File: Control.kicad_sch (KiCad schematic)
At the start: 65 parts, among them U2 LT6108IMS8-1-TRPBF, U3 LM139ADRG4, U5 LT6108IMS8-1-TRPBF

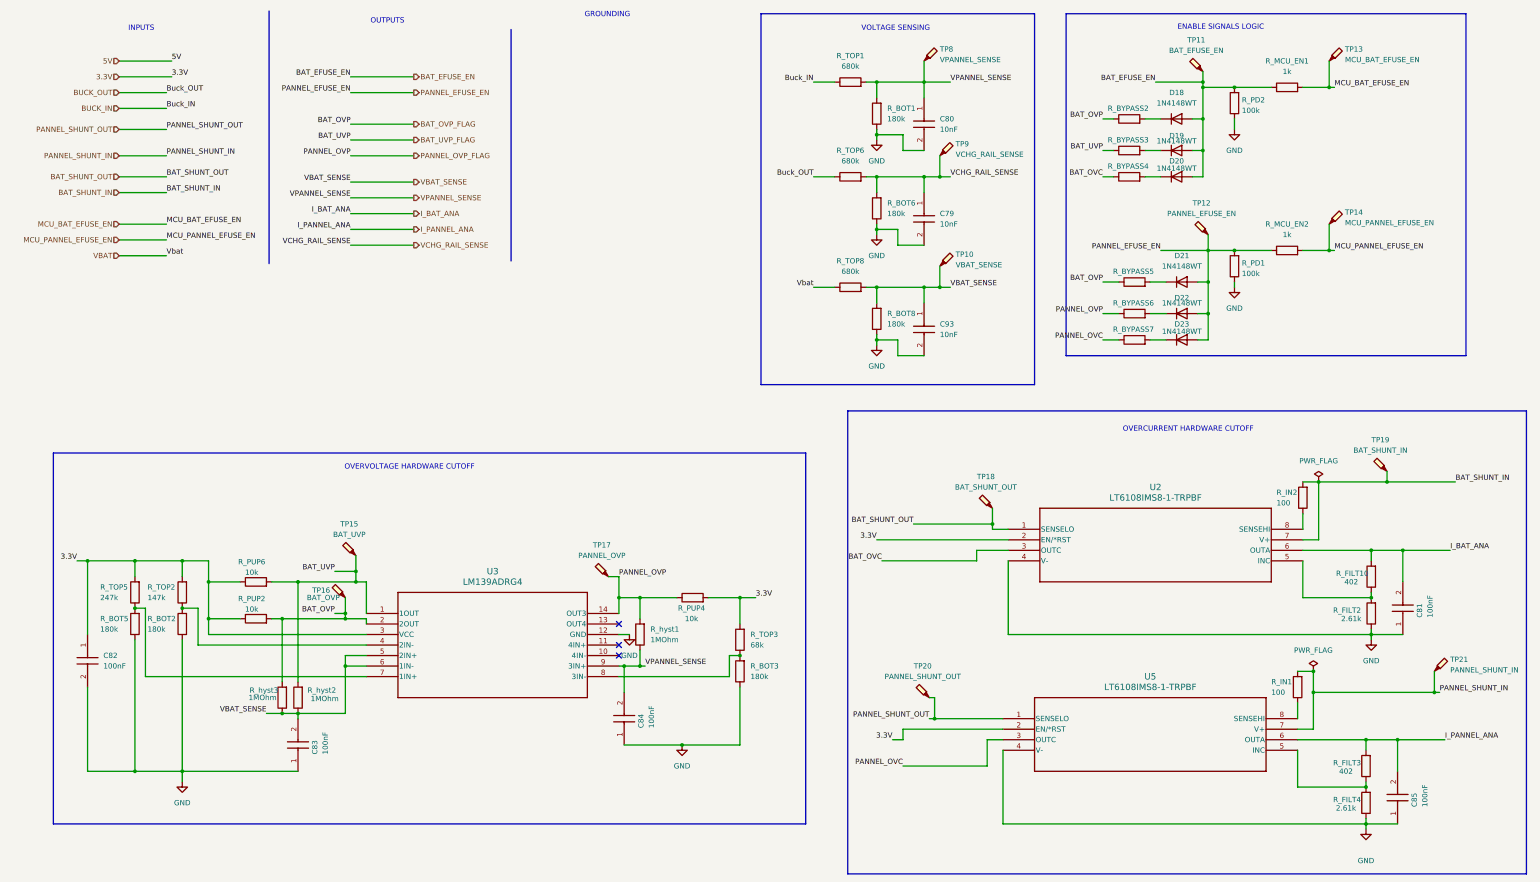
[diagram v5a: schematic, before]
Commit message: changed mcu power suppl
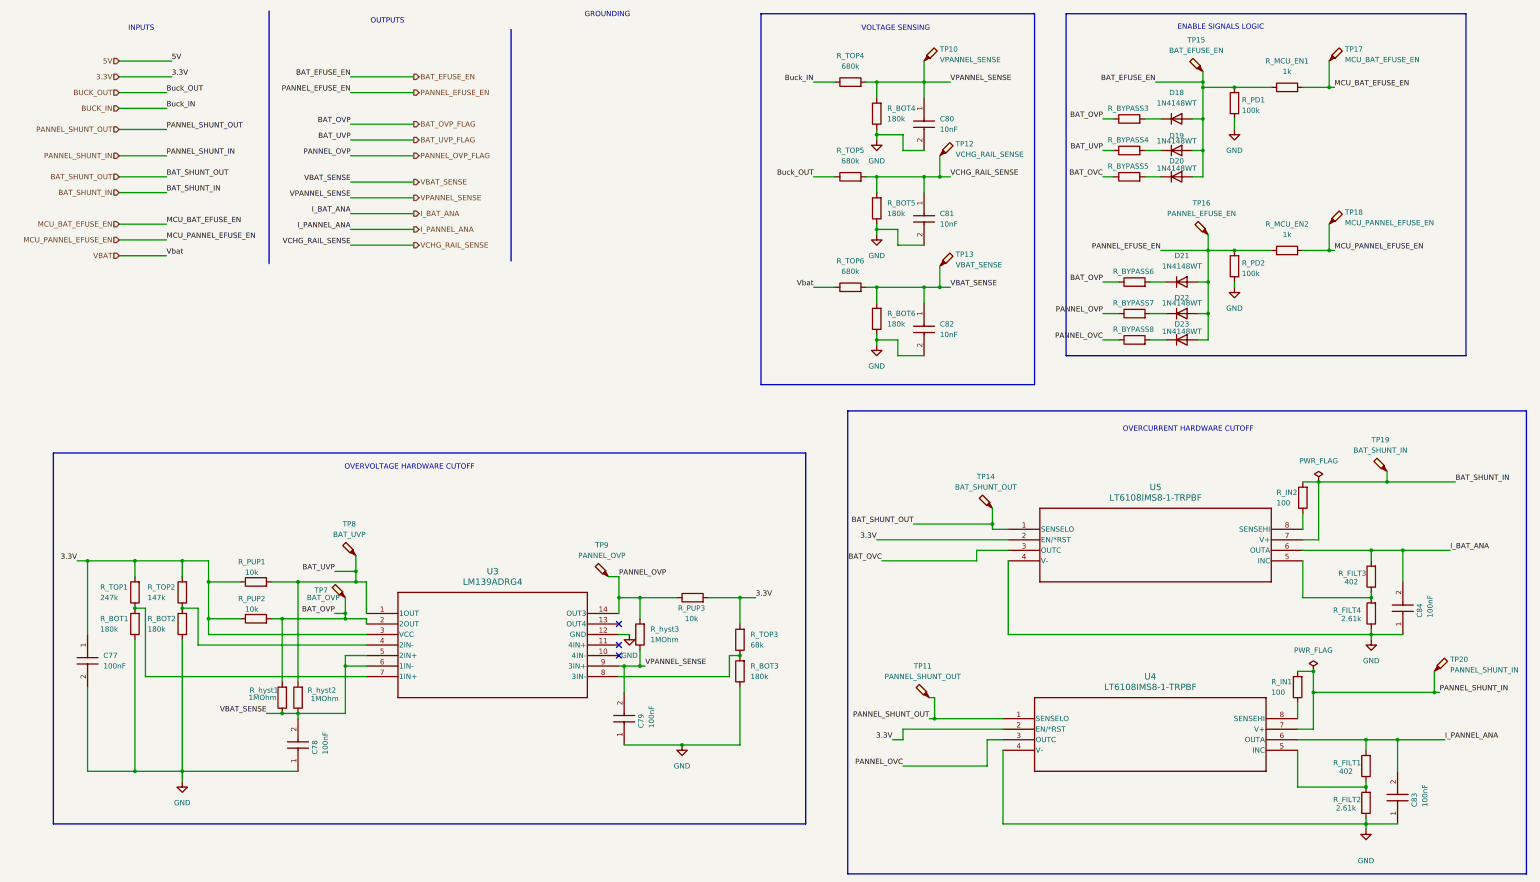
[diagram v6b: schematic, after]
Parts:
- renumbered C82 to C77, C83 to C78, C84 to C79, C79 to C81, C93 to C82, C85 to C83, C81 to C84, R_BOT5 to R_BOT1, R_BOT1 to R_BOT4, R_BOT6 to R_BOT5, R_BOT8 to R_BOT6, R_BYPASS2 to R_BYPASS3, R_BYPASS3 to R_BYPASS4, R_BYPASS4 to R_BYPASS5, R_BYPASS5 to R_BYPASS6, R_BYPASS6 to R_BYPASS7, R_BYPASS7 to R_BYPASS8, R_FILT3 to R_FILT1, R_FILT4 to R_FILT2, R_FILT10 to R_FILT3, R_FILT2 to R_FILT4, R_PD2 to R_PD1, R_PD1 to R_PD2, R_PUP6 to R_PUP1, R_PUP4 to R_PUP3, R_TOP5 to R_TOP1, R_TOP1 to R_TOP4, R_TOP6 to R_TOP5, R_TOP8 to R_TOP6, R_hyst3 to R_hyst1, R_hyst1 to R_hyst3, TP8 to TP10, TP20 to TP11, TP9 to TP12, TP10 to TP13, TP18 to TP14, TP11 to TP15, TP12 to TP16, TP13 to TP17, TP14 to TP18, TP21 to TP20, TP16 to TP7, TP15 to TP8, TP17 to TP9, U5 to U4, U2 to U5
